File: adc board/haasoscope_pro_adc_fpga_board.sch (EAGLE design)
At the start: 588 parts, among them CN2 12Vin, IC1 ADC12DL2500ACF, IC10 TPS72325DBVR, IC11 LM393D, IC13 LMH5401IRMST, IC14 LMH6401IRMZR, IC15 SN74AVC4T774PWR, IC17 DAC8562SDGSR, IC18 TLV9102IPWR, IC2 SN74AVC4T774PWR, IC21 LMH5401IRMST, IC22 TPS7A7200RGTR, IC23 TPS7A7200RGTR, IC24 TPS7A7200RGTR, IC25 TPS72325DBVR, IC26 TPS7A7200RGTR, IC27 TPS7A7200RGTR, IC28 TPS7A7200RGTR, IC29 LMH6401IRMZR, IC3 ADC122S021CIMM_NOPB, IC30 SN74AVC4T774PWR, IC33 TLV9102IPWR, IC4 TLV9102IPWR, IC5 EP4CE30F23C6N, IC6 EPCQ16ASI8N, IC7 TPS7A7200RGTR, IC8 FT232HQ, IC9 93LC56B, J1 2p-2.54, J10 8pin, J11 8pin, J13 8pin, J15 test1, J2 test1, J3 2p-2.54, J30 2p-2.54, J31 2p-2.54, J32 2p-2.54, J33 2p-2.54, J34 2p-2.54, J35 2p-2.54, J36 2p-2.54, J37 2p-2.54, J39 2p-2.54, J4 2p-2.54, J40 2p-2.54, J41 2p-2.54, J42 2p-2.54, J43 2p-2.54, J44 2p-2.54, J45 2p-2.54, J46 2p-2.54, J8 8pin, K1 G6K-2F-RF-T-TR03_DC5, K2 G6K-2F-RF-T-TR03_DC5, K3 G6K-2F-RF-T-TR03_DC5, K4 G6K-2F-RF-T-TR03_DC5, K5 G6K-2F-RF-T-TR03_DC5, K6 TLP3475R_TP,F, K7 TLP3475R_TP,F, Q1 S8050, Q2 FDN340P, Q4 S8050, Q5 S8050, Q7 S8050, Q8 S8050, Q9 S8050, SW3 SKQGADE010, SW4 SKQGADE010, U2 ADF4350BCPZ, X1 USBC, Y2 OSCILLATORSMD-5X3, Y3 12MHz

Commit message: LVDS trig backwards H2/H1 outspare1 now intrigb F21/F22 inspare1 now outtrigb
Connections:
- removed net LVDSIN_SPARE1_N: IC5.IO_96, R26.2, U$1.5
- removed net LVDSIN_SPARE1_P: IC5.IO_95, R26.1, U$1.4
- removed net LVDSOUT_SPARE1_N: IC5.IO_111, U$3.5
- removed net LVDSOUT_SPARE1_P: IC5.IO_112, U$3.4
- new net LVDSIN_TRIGB_N: IC5.IO_111, R26.2, U$3.5
- new net LVDSIN_TRIGB_P: IC5.IO_112, R26.1, U$3.4
- new net LVDSOUT_TRIGB_N: IC5.IO_96, U$1.5
- new net LVDSOUT_TRIGB_P: IC5.IO_95, U$1.4

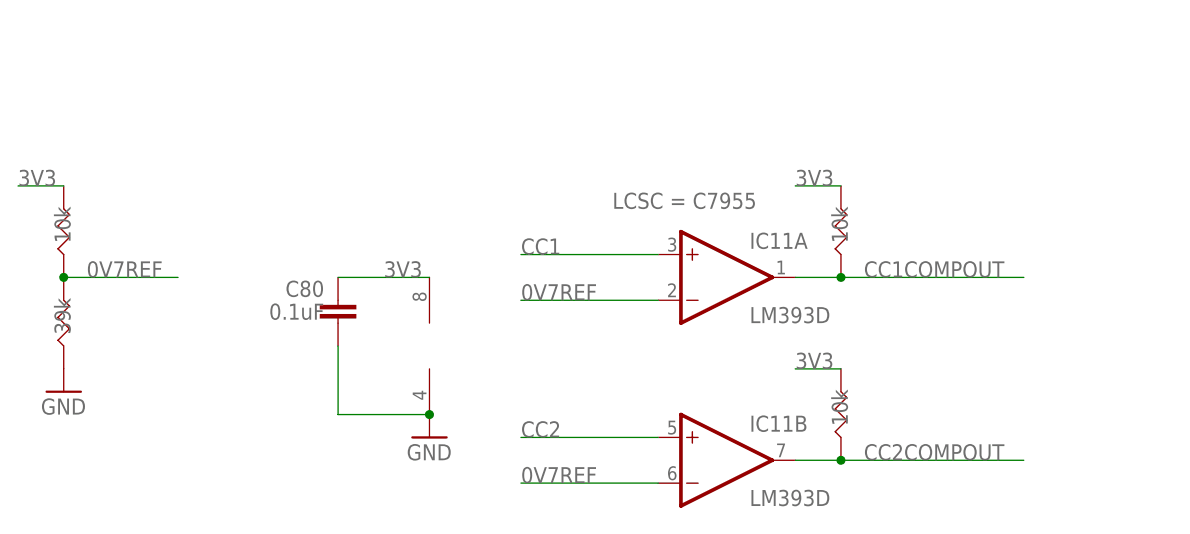
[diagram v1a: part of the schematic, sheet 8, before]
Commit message: typo in sch, remove cc1/2 comparitors, since MACs don't report correctly, and a USB A cable doesn't either
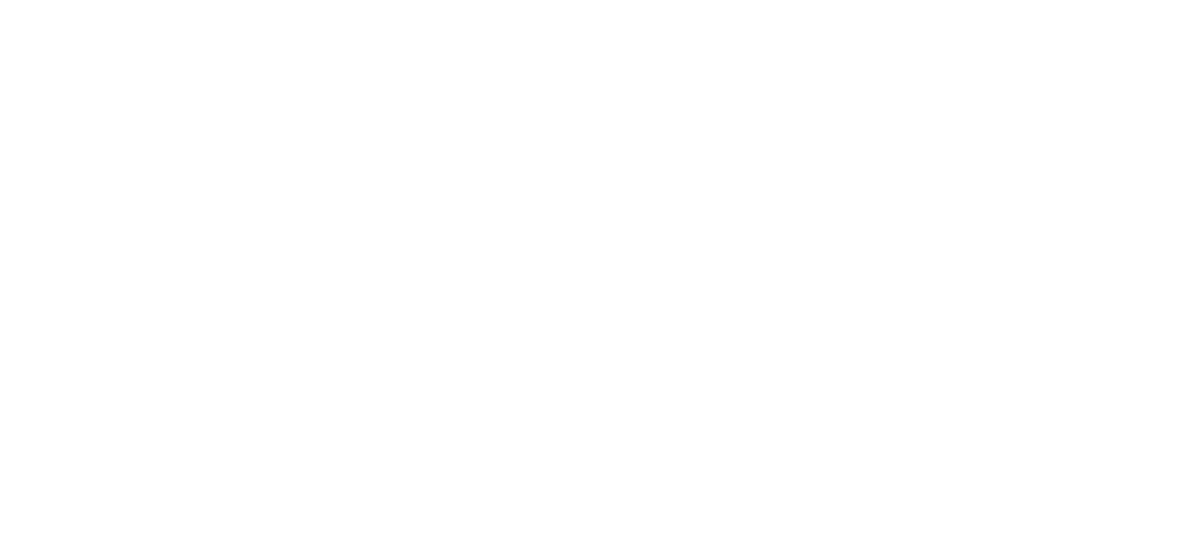
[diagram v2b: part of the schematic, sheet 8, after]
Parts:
- removed C80: 0.1uF, Nordic_nRF:CAPACITOR_0402_N
- removed IC11: LM393D, linear:LM393D
- removed R240, R241, R244: 10k, FlashPCB_Resistors:RES-0402
- removed R242, R243: 1k, FlashPCB_Resistors:RES-0402
- removed R245: 39k, FlashPCB_Resistors:RES-0402
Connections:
- removed net 0V7REF: IC11A.-IN, IC11B.-IN, R244.P$1, R245.P$2
- removed net CC1COMPOUT: IC11A.OUT, R240.P$1, R242.P$1
- removed net CC2COMPOUT: IC11B.OUT, R241.P$1, R243.P$1
- net 3V3: no longer C80.2, IC11P.V+, R240.P$2, R241.P$2, R244.P$2
- net BOARDIN0: no longer R242.P$2
- net BOARDIN1: no longer R243.P$2
- net CC1: no longer IC11A.+IN
- net CC2: no longer IC11B.+IN
- net GND: no longer C80.1, IC11P.V-, R245.P$1
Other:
- note removed: "10/(10+39) * 3.3V = 0.67V"
- note removed: "CC1 or 2 indicate USB C polarity Read the voltage on CC1/2, if it is >0.7V, you can draw 1.5A @5V (USB Type-C Spec R2.0 - August 2019 page 241) >1.31V, you can draw 3A @5V"
- note removed: "Comparitors for some analog signals, whose outputs get fed to FPGA"
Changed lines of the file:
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@@
 <part name="R238" library="FlashPCB_Resistors" deviceset="RES-0402" device="" value="1k"/>
 <part name="R239" library="FlashPCB_Resistors" deviceset="RES-0402" device="" value="10k"/>
-<part name="IC11" library="linear" library_urn="urn:adsk.eagle:library:262" deviceset="LM393" device="D" package3d_urn="urn:adsk.eagle:package:16404/2">
-<attribute name="LCSC" value="C7955"/>
-</part>
-<part name="C80" library="Nordic_nRF" library_urn="urn:adsk.eagle:library:169009" deviceset="CAPACITOR" device="_0402_N" package3d_urn="urn:adsk.eagle:package:2593732/1" value="0.1uF"/>
-<part name="GND63" library="supply1" deviceset="GND" device=""/>
-<part name="R240" library="FlashPCB_Resistors" deviceset="RES-0402" device="" value="10k"/>
-<part name="R241" library="FlashPCB_Resistors" deviceset="RES-0402" device="" value="10k"/>
-<part name="R242" library="FlashPCB_Resistors" deviceset="RES-0402" device="" value="1k"/>
-<part name="R243" library="FlashPCB_Resistors" deviceset="RES-0402" device="" value="1k"/>
-<part name="R244" library="FlashPCB_Resistors" deviceset="RES-0402" device="" value="10k"/>
-<part name="R245" library="FlashPCB_Resistors" deviceset="RES-0402" device="" value="39k"/>
-<part name="GND64" library="supply1" deviceset="GND" device=""/>
 </parts>
 <sheets>
@@
 <attribute name="VALUE" x="107.95" y="573.278" size="1.778" layer="96"/>
 </instance>
-<instance part="R242" gate="G$1" x="109.22" y="579.12" smashed="yes">
-<attribute name="VALUE" x="107.95" y="578.358" size="1.778" layer="96"/>
-</instance>
-<instance part="R243" gate="G$1" x="109.22" y="576.58" smashed="yes">
-<attribute name="VALUE" x="107.95" y="575.818" size="1.778" layer="96"/>
-</instance>
 </instances>
 <busses>
@@
 <wire x1="129.54" y1="576.58" x2="114.3" y2="576.58" width="0.1524" layer="91"/>
 <label x="114.3" y="576.58" size="1.778" layer="95"/>
-<pinref part="R243" gate="G$1" pin="P$2"/>
 </segment>
 </net>
@@
 <wire x1="129.54" y1="579.12" x2="114.3" y2="579.12" width="0.1524" layer="91"/>
 <label x="114.3" y="579.12" size="1.778" layer="95"/>
-<pinref part="R242" gate="G$1" pin="P$2"/>
 </segment>
 </net>
@@
 </segment>
 </net>
-<net name="CC1COMPOUT" class="0">
-<segment>
-<pinref part="R242" gate="G$1" pin="P$1"/>
-<wire x1="78.74" y1="579.12" x2="104.14" y2="579.12" width="0.1524" layer="91"/>
-<label x="78.74" y="579.12" size="1.778" layer="95"/>
-</segment>
-</net>
-<net name="CC2COMPOUT" class="0">
-<segment>
-<pinref part="R243" gate="G$1" pin="P$1"/>
-<wire x1="104.14" y1="576.58" x2="78.74" y2="576.58" width="0.1524" layer="91"/>
-<label x="78.74" y="576.58" size="1.778" layer="95"/>
-</segment>
-</net>
 <net name="LVDSIN_TRIGB_N" class="2">
 <segment>
@@
 If 12VConnected is high (5V), then switch is off
 If 12VConnected is low (0V), then switch is on</text>
-<text x="-68.58" y="-12.7" size="1.778" layer="90">Comparitors for some analog signals,
-whose outputs get fed to FPGA</text>
-<text x="-73.66" y="-71.12" size="1.778" layer="90">CC1 or 2 indicate USB C polarity
-Read the voltage on CC1/2, if it is
-&gt;0.7V, you can draw 1.5A @5V
-(USB Type-C Spec R2.0 - August 2019 page 241)
-&gt;1.31V, you can draw 3A @5V</text>
-<text x="-116.84" y="-45.72" size="1.778" layer="90">10/(10+39) * 3.3V = 0.67V</text>
 </plain>
 <instances>
@@
 <attribute name="VALUE" x="-47.498" y="46.99" size="1.778" layer="96" rot="R90"/>
 </instance>
-<instance part="IC11" gate="A" x="-30.48" y="-25.4" smashed="yes">
-<attribute name="NAME" x="-27.94" y="-22.225" size="1.778" layer="95"/>
-<attribute name="VALUE" x="-27.94" y="-30.48" size="1.778" layer="96"/>
-<attribute name="LCSC" x="-43.18" y="-17.78" size="1.778" layer="96" display="both"/>
-</instance>
-<instance part="IC11" gate="B" x="-30.48" y="-45.72" smashed="yes">
-<attribute name="NAME" x="-27.94" y="-42.545" size="1.778" layer="95"/>
-<attribute name="VALUE" x="-27.94" y="-50.8" size="1.778" layer="96"/>
-</instance>
-<instance part="IC11" gate="P" x="-63.5" y="-33.02" smashed="yes"/>
-<instance part="C80" gate="C$1" x="-73.66" y="-30.48" smashed="yes" rot="R180">
-<attribute name="NAME" x="-75.184" y="-25.781" size="1.778" layer="95" rot="R180"/>
-<attribute name="VALUE" x="-75.184" y="-28.321" size="1.778" layer="96" rot="R180"/>
-</instance>
-<instance part="GND63" gate="1" x="-63.5" y="-43.18" smashed="yes">
-<attribute name="VALUE" x="-66.04" y="-45.72" size="1.778" layer="96"/>
-</instance>
-<instance part="R240" gate="G$1" x="-17.78" y="-20.32" smashed="yes" rot="R90">
-<attribute name="VALUE" x="-17.018" y="-21.59" size="1.778" layer="96" rot="R90"/>
-</instance>
-<instance part="R241" gate="G$1" x="-17.78" y="-40.64" smashed="yes" rot="R90">
-<attribute name="VALUE" x="-17.018" y="-41.91" size="1.778" layer="96" rot="R90"/>
-</instance>
-<instance part="R244" gate="G$1" x="-104.14" y="-20.32" smashed="yes" rot="R90">
-<attribute name="VALUE" x="-103.378" y="-21.59" size="1.778" layer="96" rot="R90"/>
-</instance>
-<instance part="R245" gate="G$1" x="-104.14" y="-30.48" smashed="yes" rot="R90">
-<attribute name="VALUE" x="-103.378" y="-31.75" size="1.778" layer="96" rot="R90"/>
-</instance>
-<instance part="GND64" gate="1" x="-104.14" y="-38.1" smashed="yes">
-<attribute name="VALUE" x="-106.68" y="-40.64" size="1.778" layer="96"/>
-</instance>
 </instances>
 <busses>
@@
 <wire x1="81.28" y1="22.86" x2="81.28" y2="27.94" width="0.1524" layer="91"/>
 </segment>
-<segment>
-<pinref part="IC11" gate="P" pin="V-"/>
-<pinref part="GND63" gate="1" pin="GND"/>
-<wire x1="-73.66" y1="-33.02" x2="-73.66" y2="-40.64" width="0.1524" layer="91"/>
-<wire x1="-73.66" y1="-40.64" x2="-63.5" y2="-40.64" width="0.1524" layer="91"/>
-<junction x="-63.5" y="-40.64"/>
-<pinref part="C80" gate="C$1" pin="1"/>
-</segment>
-<segment>
-<pinref part="R245" gate="G$1" pin="P$1"/>
-<pinref part="GND64" gate="1" pin="GND"/>
-</segment>
 </net>
 <net name="USB_D_N" class="3">
@@
 <pinref part="R183" gate="G$1" pin="P$2"/>
 </segment>
-<segment>
-<pinref part="IC11" gate="A" pin="+IN"/>
-<wire x1="-38.1" y1="-22.86" x2="-53.34" y2="-22.86" width="0.1524" layer="91"/>
-<label x="-53.34" y="-22.86" size="1.778" layer="95"/>
-</segment>
 </net>
 <net name="CC2" class="0">
@@
 <pinref part="R182" gate="G$1" pin="P$2"/>
 </segment>
-<segment>
-<pinref part="IC11" gate="B" pin="+IN"/>
-<wire x1="-38.1" y1="-43.18" x2="-53.34" y2="-43.18" width="0.1524" layer="91"/>
-<label x="-53.34" y="-43.18" size="1.778" layer="95"/>
-</segment>
 </net>
 <net name="VCC3V3" class="0">
@@
 <label x="170.18" y="66.04" size="1.778" layer="95"/>
 </segment>
-<segment>
-<wire x1="-73.66" y1="-25.4" x2="-63.5" y2="-25.4" width="0.1524" layer="91"/>
-<pinref part="IC11" gate="P" pin="V+"/>
-<pinref part="C80" gate="C$1" pin="2"/>
-<label x="-68.58" y="-25.4" size="1.778" layer="95"/>
-</segment>
-<segment>
-<wire x1="-22.86" y1="-15.24" x2="-17.78" y2="-15.24" width="0.1524" layer="91"/>
-<pinref part="R240" gate="G$1" pin="P$2"/>
-<label x="-22.86" y="-15.24" size="1.778" layer="95"/>
-</segment>
-<segment>
-<wire x1="-22.86" y1="-35.56" x2="-17.78" y2="-35.56" width="0.1524" layer="91"/>
-<pinref part="R241" gate="G$1" pin="P$2"/>
-<label x="-22.86" y="-35.56" size="1.778" layer="95"/>
-</segment>
-<segment>
-<wire x1="-109.22" y1="-15.24" x2="-104.14" y2="-15.24" width="0.1524" layer="91"/>
-<pinref part="R244" gate="G$1" pin="P$2"/>
-<label x="-109.22" y="-15.24" size="1.778" layer="95"/>
-</segment>
 </net>
 <net name="FTDI_DATA1" class="5">
@@
 </segment>
 </net>
-<net name="CC1COMPOUT" class="0">
-<segment>
-<pinref part="IC11" gate="A" pin="OUT"/>
-<wire x1="-22.86" y1="-25.4" x2="-17.78" y2="-25.4" width="0.1524" layer="91"/>
-<pinref part="R240" gate="G$1" pin="P$1"/>
-<wire x1="-17.78" y1="-25.4" x2="2.54" y2="-25.4" width="0.1524" layer="91"/>
-<junction x="-17.78" y="-25.4"/>
-<label x="-15.24" y="-25.4" size="1.778" layer="95"/>
-</segment>
-</net>
-<net name="CC2COMPOUT" class="0">
-<segment>
-<wire x1="-22.86" y1="-45.72" x2="-17.78" y2="-45.72" width="0.1524" layer="91"/>
-<pinref part="R241" gate="G$1" pin="P$1"/>
-<wire x1="-17.78" y1="-45.72" x2="2.54" y2="-45.72" width="0.1524" layer="91"/>
-<junction x="-17.78" y="-45.72"/>
-<pinref part="IC11" gate="B" pin="OUT"/>
-<label x="-15.24" y="-45.72" size="1.778" layer="95"/>
-</segment>
-</net>
-<net name="0V7REF" class="0">
-<segment>
-<pinref part="IC11" gate="A" pin="-IN"/>
-<wire x1="-38.1" y1="-27.94" x2="-53.34" y2="-27.94" width="0.1524" layer="91"/>
-<label x="-53.34" y="-27.94" size="1.778" layer="95"/>
-</segment>
-<segment>
-<pinref part="IC11" gate="B" pin="-IN"/>
-<wire x1="-38.1" y1="-48.26" x2="-53.34" y2="-48.26" width="0.1524" layer="91"/>
-<label x="-53.34" y="-48.26" size="1.778" layer="95"/>
-</segment>
-<segment>
-<pinref part="R244" gate="G$1" pin="P$1"/>
-<wire x1="-104.14" y1="-25.4" x2="-91.44" y2="-25.4" width="0.1524" layer="91"/>
-<pinref part="R245" gate="G$1" pin="P$2"/>
-<junction x="-104.14" y="-25.4"/>
-<label x="-101.6" y="-25.4" size="1.778" layer="95"/>
-</segment>
-</net>
 </nets>
 </sheet>
@@
 </sheet>
 <sheet>
-<description>Power - Amps and 12V</description>
+<description>Power - Amps</description>
 <plain>
 <text x="93.98" y="198.12" size="1.778" layer="90">V- for input amp reg ~ -3.0V</text>

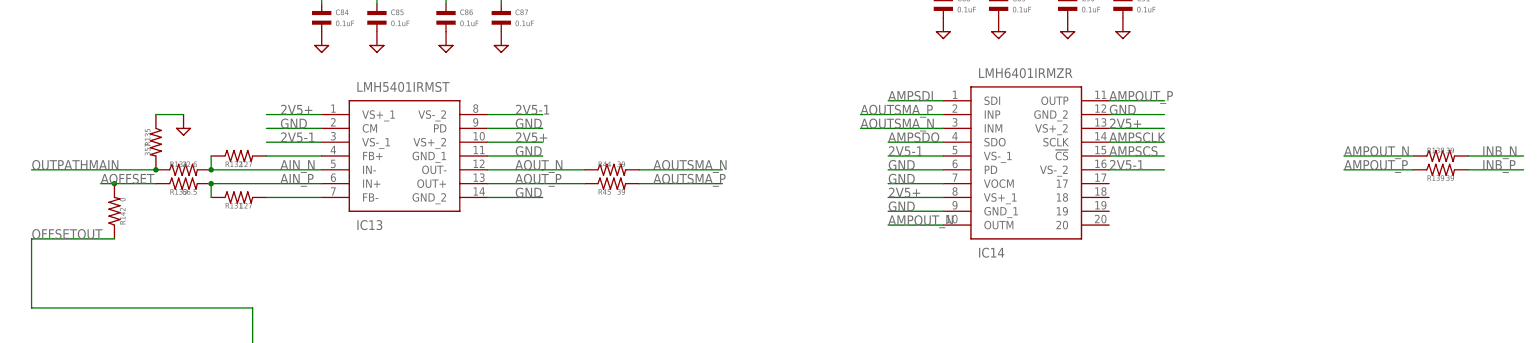
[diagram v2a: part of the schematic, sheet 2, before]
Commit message: cutout gnd on top layer below sma other minor aesthetic changes
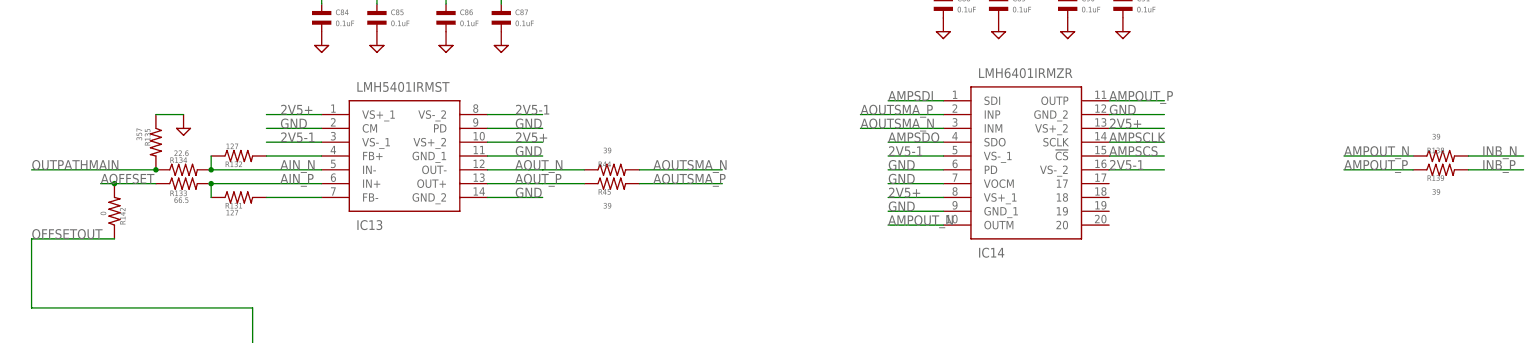
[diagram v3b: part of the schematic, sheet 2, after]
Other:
- note added: "Nearly identical to preinput for channel 1, except there's no split out See comments on sheet 1 for details"
- note added: "RC freq for 50 Ohm * 1uF is ~3kHz, so frequencies less than that will be filtered Z~1.5 Ohm at 2 GHz for CL05A105KA5NQNC"
- note removed: "Z~1.5 Ohm at 2 GHz for CL05A105KA5NQNC"

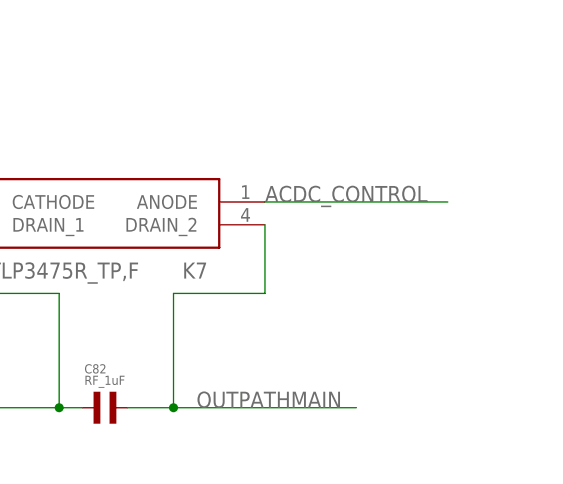
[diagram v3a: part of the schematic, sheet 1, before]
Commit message: switch to TLP3475 from TLP3475, because of availability
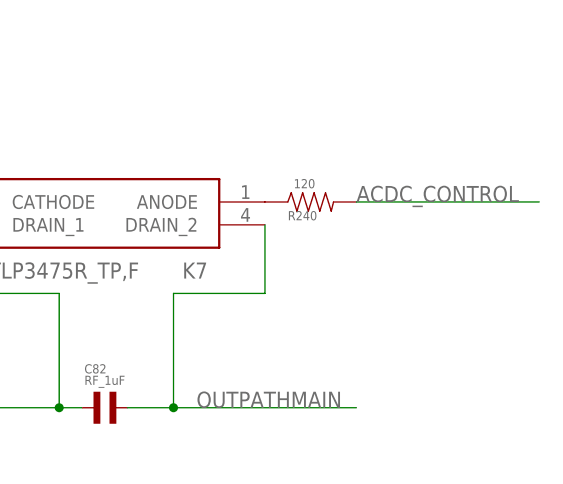
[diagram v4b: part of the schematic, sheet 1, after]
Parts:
- added R240, R241: 120, MF_Passives:RESISTOR_0402
- K6, K7: MANUFACTURER_PART_NUMBER TLP3475R(TP,F -> TLP3475; MOUSER_PART_NUMBER (none) -> 757-TLP3475
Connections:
- new net N$64: K7.ANODE, R240.P$1
- new net N$66: K6.ANODE, R241.P$1
- net ACDC_CONTROL: now also R240.P$2; no longer K7.ANODE
- net ACDC_CONTROL2: now also R241.P$2; no longer K6.ANODE
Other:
- note added: "I=10mA suggested 2.5V - 1.3V forward voltage drop = 1.2V 1.2V/120Ohm=10mA"
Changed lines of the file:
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@@
 <part name="SUPPLY19" library="supply2" library_urn="urn:adsk.eagle:library:372" deviceset="GND" device=""/>
 <part name="K6" library="TLP3475R_TP_F" deviceset="TLP3475R_TP,F" device="">
-<attribute name="MANUFACTURER_PART_NUMBER" value="TLP3475R(TP,F"/>
+<attribute name="MANUFACTURER_PART_NUMBER" value="TLP3475"/>
+<attribute name="MOUSER_PART_NUMBER" value="757-TLP3475"/>
 </part>
 <part name="SUPPLY20" library="supply2" library_urn="urn:adsk.eagle:library:372" deviceset="GND" device=""/>
 <part name="K7" library="TLP3475R_TP_F" deviceset="TLP3475R_TP,F" device="">
-<attribute name="MANUFACTURER_PART_NUMBER" value="TLP3475R(TP,F"/>
+<attribute name="MANUFACTURER_PART_NUMBER" value="TLP3475"/>
+<attribute name="MOUSER_PART_NUMBER" value="757-TLP3475"/>
 </part>
 <part name="R31" library="FlashPCB_Resistors" deviceset="RES-0402" device="" value="47"/>
@@
 <part name="R238" library="FlashPCB_Resistors" deviceset="RES-0402" device="" value="1k"/>
 <part name="R239" library="FlashPCB_Resistors" deviceset="RES-0402" device="" value="10k"/>
+<part name="R240" library="MF_Passives" deviceset="RESISTOR" device="_0402" value="120"/>
+<part name="R241" library="MF_Passives" deviceset="RESISTOR" device="_0402" value="120"/>
 </parts>
 <sheets>
@@
 <text x="337.82" y="213.36" size="1.778" layer="90">To input amps
 on next sheet</text>
+<text x="322.58" y="236.22" size="1.778" layer="90">I=10mA suggested
+2.5V - 1.3V forward voltage drop = 1.2V
+1.2V/120Ohm=10mA</text>
 </plain>
 <instances>
@@
 </instance>
 <instance part="SUPPLY6" gate="GND" x="20.32" y="243.84" smashed="yes"/>
+<instance part="R240" gate="G$1" x="325.12" y="246.38" smashed="yes" rot="R90">
+<attribute name="NAME" x="322.58" y="245.364" size="1.016" layer="95" font="vector" align="top-left"/>
+<attribute name="VALUE" x="325.628" y="248.92" size="1.016" layer="96" font="vector" rot="R180"/>
+</instance>
 </instances>
 <busses>
@@
 </segment>
 </net>
-<net name="ACDC_CONTROL" class="0">
-<segment>
-<wire x1="340.36" y1="246.38" x2="320.04" y2="246.38" width="0.1524" layer="91"/>
-<label x="320.04" y="246.38" size="1.778" layer="95"/>
-<pinref part="K7" gate="G$1" pin="ANODE"/>
-</segment>
-</net>
 <net name="50_1M_CONTROL" class="0">
 <segment>
@@
 <label x="76.2" y="172.72" size="1.778" layer="95"/>
 <pinref part="K2" gate="G$1" pin="COM_1"/>
+</segment>
+</net>
+<net name="N$64" class="0">
+<segment>
+<pinref part="K7" gate="G$1" pin="ANODE"/>
+<pinref part="R240" gate="G$1" pin="P$1"/>
+</segment>
+</net>
+<net name="ACDC_CONTROL" class="0">
+<segment>
+<wire x1="350.52" y1="246.38" x2="330.2" y2="246.38" width="0.1524" layer="91"/>
+<label x="330.2" y="246.38" size="1.778" layer="95"/>
+<pinref part="R240" gate="G$1" pin="P$2"/>
 </segment>
 </net>
@@
 <attribute name="VALUE" x="278.13" y="200.66" size="1.778" layer="96" rot="R180" align="center-left"/>
 </instance>
+<instance part="R241" gate="G$1" x="297.18" y="208.28" smashed="yes" rot="R90">
+<attribute name="NAME" x="294.64" y="207.264" size="1.016" layer="95" font="vector" align="top-left"/>
+<attribute name="VALUE" x="299.72" y="207.264" size="1.016" layer="96" font="vector" rot="R180"/>
+</instance>
 </instances>
 <busses>
@@
 </segment>
 </net>
-<net name="ACDC_CONTROL2" class="0">
-<segment>
-<wire x1="312.42" y1="208.28" x2="292.1" y2="208.28" width="0.1524" layer="91"/>
-<label x="292.1" y="208.28" size="1.778" layer="95"/>
-<pinref part="K6" gate="G$1" pin="ANODE"/>
-</segment>
-</net>
 <net name="50_1M_CONTROL2" class="0">
 <segment>
@@
 </segment>
 </net>
+<net name="N$66" class="0">
+<segment>
+<pinref part="K6" gate="G$1" pin="ANODE"/>
+<pinref part="R241" gate="G$1" pin="P$1"/>
+</segment>
+</net>
+<net name="ACDC_CONTROL2" class="0">
+<segment>
+<wire x1="322.58" y1="208.28" x2="302.26" y2="208.28" width="0.1524" layer="91"/>
+<label x="302.26" y="208.28" size="1.778" layer="95"/>
+<pinref part="R241" gate="G$1" pin="P$2"/>
+</segment>
+</net>

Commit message: cleanup schematics
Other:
- note added: "Amplify temp signals so they're in a good range for the slow ADC"
- note removed: "Amplify temp signals so they're in a good range for the slow adc"
- note removed: "RF relay"
- moved on the sheet: BNCIN1, BNCIN2, C55, C56, C57, C72, C75, C78, C79, C82, FL2, FL3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
